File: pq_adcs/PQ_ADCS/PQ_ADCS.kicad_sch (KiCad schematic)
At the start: 51 parts, among them J1 CES-110-02-L-S, J10 Pico-Clasp_01x09, J11 Pico-Clasp_01x15, J12 CES-102-02-L-S, J2 CES-110-02-L-S, J3 CES-110-02-L-S, J4 CES-110-02-L-S, J5 Pico-Clasp_01x03, J6 Pico-Clasp_01x10, J7 Pico-Clasp_01x10, J8 Pico-Clasp_01x10, J9 Pico-Clasp_01x10, U1 LPV542, U2 LPV542, U3 LPV542, U4 IIM-42652, U5 BD2606MVV, U6 TMUX1108RSVR, U7 MMC5983MA

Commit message: fabrication
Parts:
- Annotation1: footprint -nsl_symbols:Bike -> symbols-nsl:Bike
- Annotation2: footprint -nsl_symbols:Bridgemaker -> symbols-nsl:Bridgemaker
- J1, J2, J3, J4: footprint -nsl_connector:SLW-110-01 -> connector-nsl:SLW-110-01
- J10: footprint -nsl_connector:Picoclasp09 -> connector-nsl:Picoclasp09
- J11: footprint -nsl_connector:Picoclasp15 -> connector-nsl:Picoclasp15
- J12: footprint -nsl_connector:CES-102-02 -> connector-nsl:CES-102-02
- J5: footprint -nsl_connector:Picoclasp03 -> connector-nsl:Picoclasp03
- J6, J7, J8, J9: footprint -nsl_connector:Picoclasp10 -> connector-nsl:Picoclasp10
- U2, U3: footprint -nsl_miscellaneous:TI_X1SON-8_3x3mm -> miscelaneous-nsl:TI_X1SON-8_3x3mm
- U6: footprint -nsl_miscellaneous:UQFN-16_1.8x2.6_Pitch0.4mm -> miscelaneous-nsl:UQFN-16_1.8x2.6_Pitch0.4mm
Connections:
- net GND: no longer J11.9
- net STM32_PB3: now also J11.9
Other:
- moved on the sheet: J10, J11, J12, J5, J6, J7, J8, J9

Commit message: BOM creation schematic changes 2.0
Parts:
- H1, H2, H3, H4: Manufacturer 1 - -> N/A; Manufacturer Part Number 1 - -> N/A; Supplier 1 - -> N/A; Supplier Part Number 1 - -> N/A
- U7: Manufacturer 1 (none) -> MEMSIC; Manufacturer Part Number 1 (none) -> MMC5983MA; Supplier 1 (none) -> Mouser; Supplier Part Number 1 (none) -> 438-MMC5983MA
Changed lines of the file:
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@@
       (effects (font (size 1.27 1.27)) hide)
     )
-    (property "Supplier 1" "-" (at 146.05 175.26 0)
-      (effects (font (size 1.27 1.27)) hide)
-    )
-    (property "Manufacturer 1" "-" (at 146.05 175.26 0)
-      (effects (font (size 1.27 1.27)) hide)
-    )
-    (property "Manufacturer Part Number 1" "-" (at 146.05 175.26 0)
-      (effects (font (size 1.27 1.27)) hide)
-    )
-    (property "Supplier Part Number 1" "-" (at 146.05 175.26 0)
+    (property "Supplier 1" "N/A" (at 146.05 175.26 0)
+      (effects (font (size 1.27 1.27)) hide)
+    )
+    (property "Manufacturer 1" "N/A" (at 146.05 175.26 0)
+      (effects (font (size 1.27 1.27)) hide)
+    )
+    (property "Manufacturer Part Number 1" "N/A" (at 146.05 175.26 0)
+      (effects (font (size 1.27 1.27)) hide)
+    )
+    (property "Supplier Part Number 1" "N/A" (at 146.05 175.26 0)
       (effects (font (size 1.27 1.27)) hide)
     )
@@
       (effects (font (size 1.27 1.27)) (justify left) hide)
     )
+    (property "Manufacturer 1" "MEMSIC" (at 124.46 149.86 0)
+      (effects (font (size 1.27 1.27)) hide)
+    )
+    (property "Manufacturer Part Number 1" "MMC5983MA " (at 124.46 149.86 0)
+      (effects (font (size 1.27 1.27)) hide)
+    )
+    (property "Supplier 1" "Mouser" (at 124.46 149.86 0)
+      (effects (font (size 1.27 1.27)) hide)
+    )
+    (property "Supplier Part Number 1" "438-MMC5983MA " (at 124.46 149.86 0)
+      (effects (font (size 1.27 1.27)) hide)
+    )
     (pin "1")
     (pin "10")
@@
       (effects (font (size 1.27 1.27)) hide)
     )
-    (property "Supplier 1" "-" (at 153.67 175.26 0)
-      (effects (font (size 1.27 1.27)) hide)
-    )
-    (property "Manufacturer 1" "-" (at 153.67 175.26 0)
-      (effects (font (size 1.27 1.27)) hide)
-    )
-    (property "Manufacturer Part Number 1" "-" (at 153.67 175.26 0)
-      (effects (font (size 1.27 1.27)) hide)
-    )
-    (property "Supplier Part Number 1" "-" (at 153.67 175.26 0)
+    (property "Supplier 1" "N/A" (at 153.67 175.26 0)
+      (effects (font (size 1.27 1.27)) hide)
+    )
+    (property "Manufacturer 1" "N/A" (at 153.67 175.26 0)
+      (effects (font (size 1.27 1.27)) hide)
+    )
+    (property "Manufacturer Part Number 1" "N/A" (at 153.67 175.26 0)
+      (effects (font (size 1.27 1.27)) hide)
+    )
+    (property "Supplier Part Number 1" "N/A" (at 153.67 175.26 0)
       (effects (font (size 1.27 1.27)) hide)
     )
@@
       (effects (font (size 1.27 1.27)) hide)
     )
-    (property "Supplier 1" "-" (at 138.43 175.26 0)
-      (effects (font (size 1.27 1.27)) hide)
-    )
-    (property "Manufacturer 1" "-" (at 138.43 175.26 0)
-      (effects (font (size 1.27 1.27)) hide)
-    )
-    (property "Manufacturer Part Number 1" "-" (at 138.43 175.26 0)
-      (effects (font (size 1.27 1.27)) hide)
-    )
-    (property "Supplier Part Number 1" "-" (at 138.43 175.26 0)
+    (property "Supplier 1" "N/A" (at 138.43 175.26 0)
+      (effects (font (size 1.27 1.27)) hide)
+    )
+    (property "Manufacturer 1" "N/A" (at 138.43 175.26 0)
+      (effects (font (size 1.27 1.27)) hide)
+    )
+    (property "Manufacturer Part Number 1" "N/A" (at 138.43 175.26 0)
+      (effects (font (size 1.27 1.27)) hide)
+    )
+    (property "Supplier Part Number 1" "N/A" (at 138.43 175.26 0)
       (effects (font (size 1.27 1.27)) hide)
     )
@@
       (effects (font (size 1.27 1.27)) hide)
     )
-    (property "Supplier 1" "-" (at 161.29 175.26 0)
-      (effects (font (size 1.27 1.27)) hide)
-    )
-    (property "Manufacturer 1" "-" (at 161.29 175.26 0)
-      (effects (font (size 1.27 1.27)) hide)
-    )
-    (property "Manufacturer Part Number 1" "-" (at 161.29 175.26 0)
-      (effects (font (size 1.27 1.27)) hide)
-    )
-    (property "Supplier Part Number 1" "-" (at 161.29 175.26 0)
-      (effects (font (size 1.27 1.27)) hide)
-    )
+    (property "Supplier 1" "N/A" (at 161.29 175.26 0)
+      (effects (font (size 1.27 1.27)) hide)
+    )
+    (property "Manufacturer 1" "N/A" (at 161.29 175.26 0)
+      (effects (font (size 1.27 1.27)) hide)
+    )
+    (property "Manufacturer Part Number 1" "N/A" (at 161.29 175.26 0)
+      (effects (font (size 1.27 1.27)) hide)
+    )
+    (property "Supplier Part Number 1" "N/A" (at 161.29 175.26 0)
+      (effects (font (size 1.27 1.27)) hide)
+    )

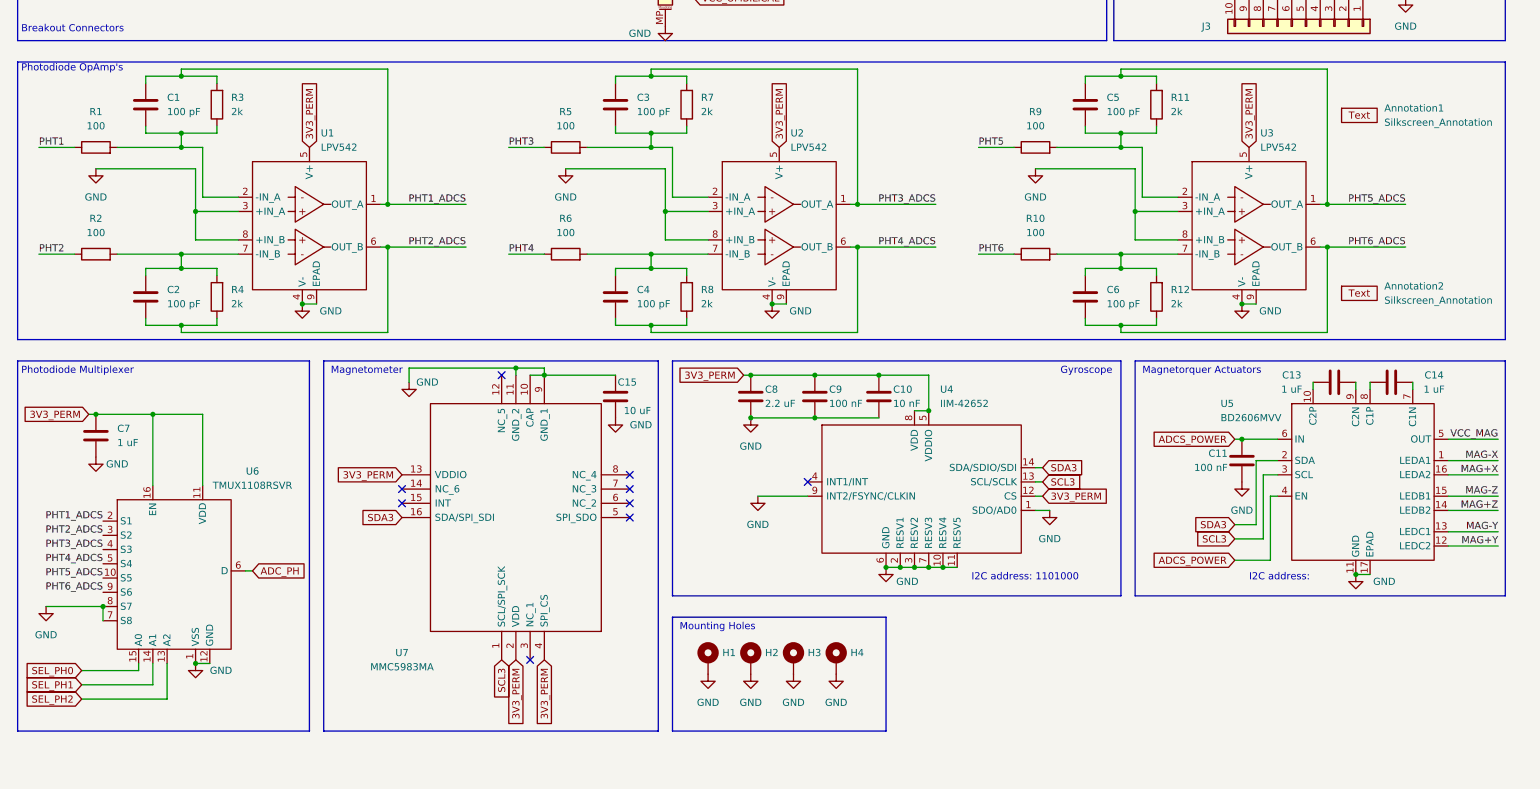
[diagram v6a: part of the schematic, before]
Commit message: opamp footprint and connections corrected
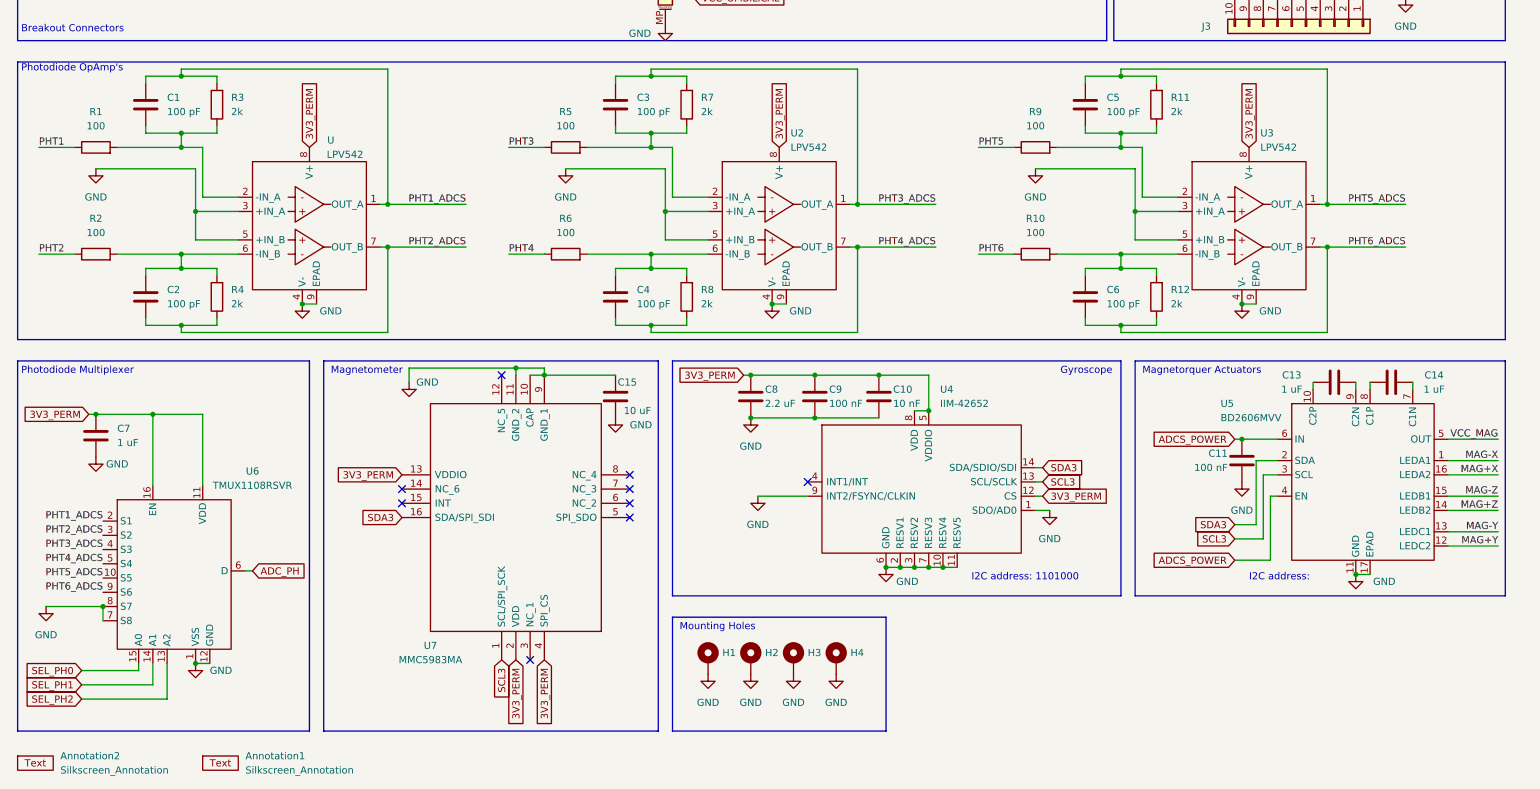
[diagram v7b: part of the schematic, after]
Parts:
- U: renamed from U1; footprint GGS_Miscellaneous:TI_X1SON-8_3x3mm -> miscellaneous-nsl:TI_X1SON-8_3x3mm; symbol GGS_Miscellaneous:LPV542 -> miscellaneous-nsl:LPV542
- U2, U3: footprint miscelaneous-nsl:TI_X1SON-8_3x3mm -> miscellaneous-nsl:TI_X1SON-8_3x3mm; symbol GGS_Miscellaneous:LPV542 -> miscellaneous-nsl:LPV542
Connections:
- net 3V3_PERM: now also U.8 (V+), U2.8 (V+), U3.8 (V+); no longer U.5 (V+), U2.5 (V+), U3.5 (V+)
- net GND: now also U.5 (+IN_B), U2.5 (+IN_B), U3.5 (+IN_B); no longer U.8 (+IN_B), U2.8 (+IN_B), U3.8 (+IN_B)
- net PHT2_ADCS: now also U.7 (OUT_B); no longer U.6 (OUT_B)
- net PHT4_ADCS: now also U2.7 (OUT_B); no longer U2.6 (OUT_B)
- net PHT6_ADCS: now also U3.7 (OUT_B); no longer U3.6 (OUT_B)
- net at C6.1, R10.2, R12.2: now also U3.6 (-IN_B); no longer U3.7 (-IN_B)
- net at C2.1, R2.2, R4.2: now also U.6 (-IN_B); no longer U.7 (-IN_B)
- net at C4.1, R6.2, R8.2: now also U2.6 (-IN_B); no longer U2.7 (-IN_B)
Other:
- moved on the sheet: Annotation1, Annotation2

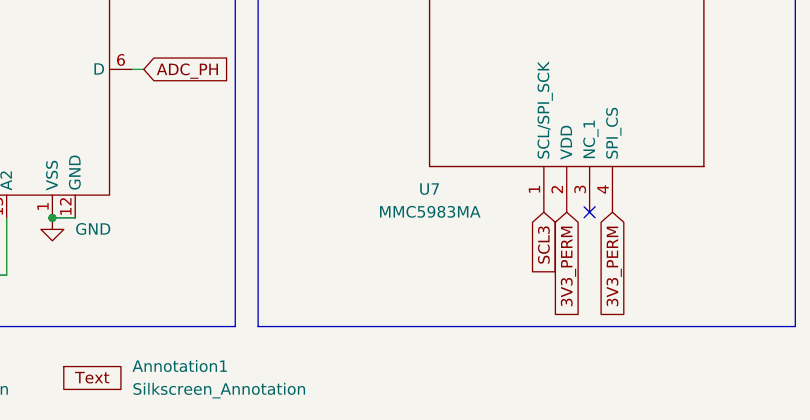
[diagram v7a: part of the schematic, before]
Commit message: added MAG addr
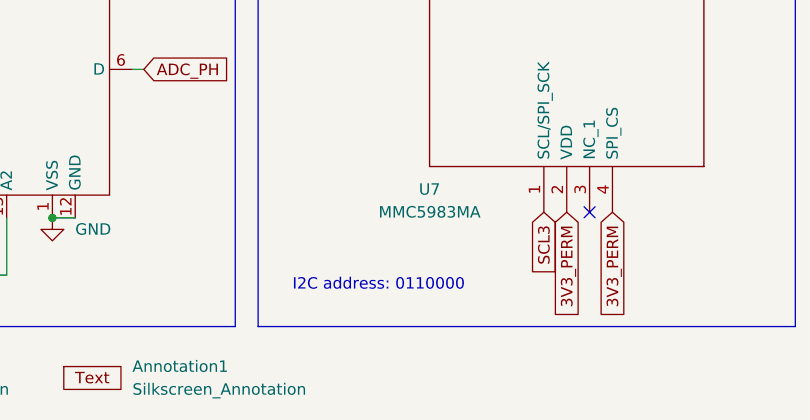
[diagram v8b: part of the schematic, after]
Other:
- note added: "I2C address: 0110000"
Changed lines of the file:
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@@
+    (effects (font (size 1.27 1.27)) (justify left bottom))
+  )
+  (text "I2C address: 0110000" (at 73.66 184.15 0)
     (effects (font (size 1.27 1.27)) (justify left bottom))
   )
